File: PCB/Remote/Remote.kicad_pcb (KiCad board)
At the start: 2 copper layers, 104.1 x 104.1 mm, 27 parts, among them J1 Barrel_Jack, J2 Joystick (Servo), J3 Joystick (Motor), M1 MountingHole_3.5mm_Pad, M2 MountingHole_3.5mm_Pad, M3 MountingHole_3.5mm_Pad, M4 MountingHole_3.5mm_Pad, SW1 Reset Button, SW2 Auto/Manual, SW3 Siren on/off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

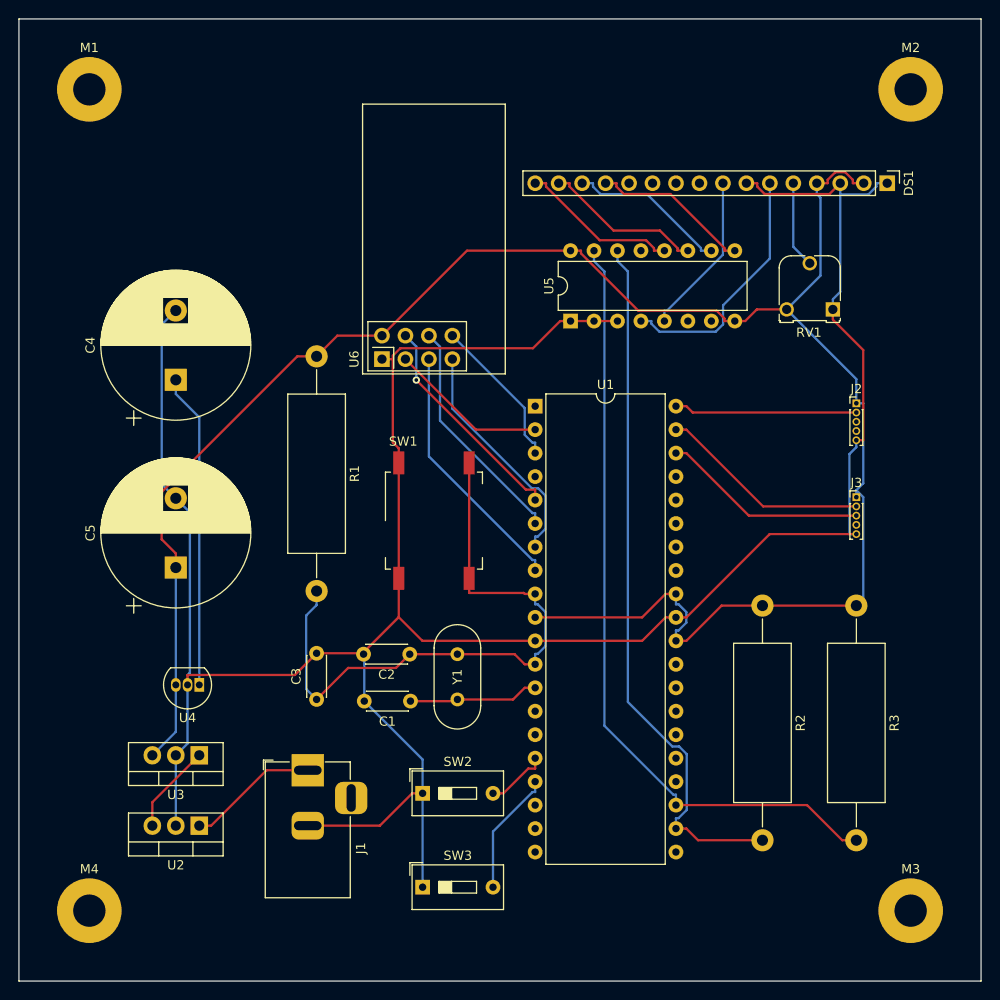
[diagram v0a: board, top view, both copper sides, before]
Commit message: 3.3v error in PCB
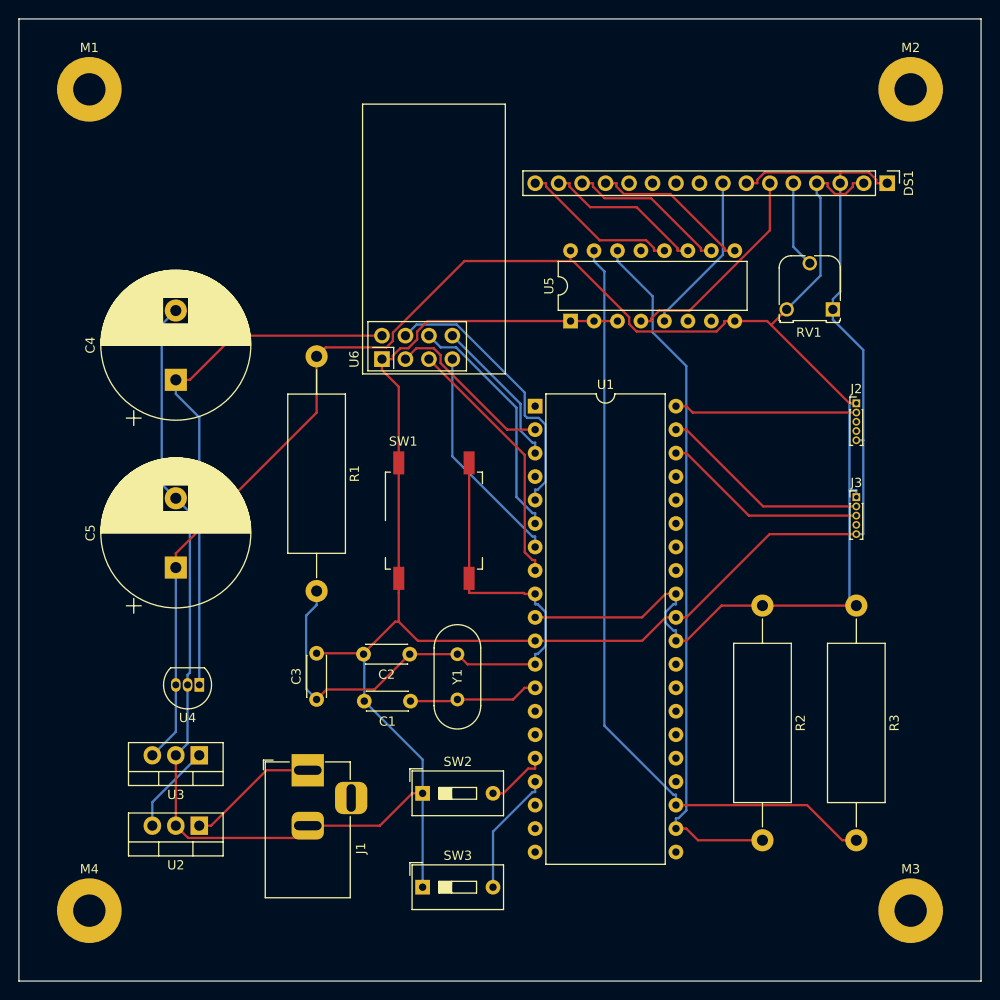
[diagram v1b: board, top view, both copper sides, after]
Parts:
- DS1: value HY1602E LCD 16x2 -> HY1602E
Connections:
- U6 pad 2: /Atmega32/5V -> /Power Supply/3.3V
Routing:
- net /Power Supply/3.3V: track 34.1 -> 58.4 mm
- net /Atmega32/CSN: track 24.2 -> 30.4 mm, vias 1 -> 0
- net Net-(DS1-Pad6): track 27.2 -> 23.3 mm
- net /Atmega32/CE: track 17.2 -> 18.7 mm
- net /Atmega32/MISO: track 25.5 -> 24.2 mm
- net /Atmega32/MOSI: track 25.3 -> 26.2 mm
- net /Atmega32/GND: track 296.3 -> 297.1 mm
- net /Atmega32/5V: track 215.9 -> 215.2 mm

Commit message: Add simulation
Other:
- board text added: "Group 47"
- board text added: "L1 Hardware Project"
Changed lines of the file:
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@@
   (gr_line (start 202.0797 139.69495) (end 97.9397 139.69495) (layer "Edge.Cuts") (width 0.1))
   (gr_line (start 202.0797 35.55495) (end 202.0797 139.69495) (layer "Edge.Cuts") (width 0.1))
+  (gr_text "Group 47" (at 171.5697 45.72) (layer "B.SilkS")
+    (effects (font (size 3 3) (thickness 0.3)) (justify mirror))
+  )
+  (gr_text "L1 Hardware Project" (at 170.18 40.64) (layer "B.SilkS")
+    (effects (font (size 2 2) (thickness 0.3)) (justify mirror))
+  )
+  (gr_text "Group 47" (at 116.84 55.88) (layer "F.SilkS")
+    (effects (font (size 3 3) (thickness 0.3)))
+  )
+  (gr_text "L1 Hardware Project" (at 116.84 50.8) (layer "F.SilkS")
+    (effects (font (size 2 2) (thickness 0.3)))
+  )
+  (dimension (type aligned) (layer "F.SilkS")
+    (pts (xy 194.4597 132.0749) (xy 194.4597 43.1749))
+    (height 13.8203)
+    (gr_text "88.9000 mm" (at 207.13 87.6249 90) (layer "F.SilkS")
+      (effects (font (size 1 1) (thickness 0.15)))
+    )
+    (format (units 3) (units_format 1) (precision 4))
+    (style (thickness 0.15) (arrow_length 1.27) (text_position_mode 0) (extension_height 0.58642) (extension_offset 0.5) keep_text_aligned)
+  )
+  (dimension (type aligned) (layer "F.SilkS")
+    (pts (xy 202.0797 35.55495) (xy 97.9397 35.55495))
+    (height 15.234949)
+    (gr_text "104.1400 mm" (at 150.0097 19.170001) (layer "F.SilkS")
+      (effects (font (size 1 1) (thickness 0.15)))
+    )
+    (format (units 3) (units_format 1) (precision 4))
+    (style (thickness 0.15) (arrow_length 1.27) (text_position_mode 0) (extension_height 0.58642) (extension_offset 0.5) keep_text_aligned)
+  )
+  (dimension (type aligned) (layer "F.SilkS")
+    (pts (xy 194.4597 43.1749) (xy 105.5597 43.1749))
+    (height 15.2349)
+    (gr_text "88.9000 mm" (at 150.0097 26.79) (layer "F.SilkS")
+      (effects (font (size 1 1) (thickness 0.15)))
+    )
+    (format (units 3) (units_format 1) (precision 4))
+    (style (thickness 0.15) (arrow_length 1.27) (text_position_mode 0) (extension_height 0.58642) (extension_offset 0.5) keep_text_aligned)
+  )
+  (dimension (type aligned) (layer "F.SilkS")
+    (pts (xy 202.0797 35.55495) (xy 194.4597 35.56))
+    (height 7.617572)
+    (gr_text "7.6200 mm" (at 198.26389 26.789905 0.03797160685) (layer "F.SilkS")
+      (effects (font (size 1 1) (thickness 0.15)))
+    )
+    (format (units 3) (units_format 1) (precision 4))
+    (style (thickness 0.15) (arrow_length 1.27) (text_position_mode 0) (extension_height 0.58642) (extension_offset 0.5) keep_text_aligned)
+  )
+  (dimension (type aligned) (layer "F.SilkS")
+    (pts (xy 198.12 139.69495) (xy 198.12 35.56))
+    (height 17.78)
+    (gr_text "104.1350 mm" (at 214.75 87.627475 90) (layer "F.SilkS")
+      (effects (font (size 1 1) (thickness 0.15)))
+    )
+    (format (units 3) (units_format 1) (precision 4))
+    (style (thickness 0.15) (arrow_length 1.27) (text_position_mode 0) (extension_height 0.58642) (extension_offset 0.5) keep_text_aligned)
+  )
+  (dimension (type aligned) (layer "F.SilkS")
+    (pts (xy 194.4597 43.1749) (xy 194.4597 35.56))
+    (height 13.8203)
+    (gr_text "7.6149 mm" (at 207.13 39.36745 90) (layer "F.SilkS")
+      (effects (font (size 1 1) (thickness 0.15)))
+    )
+    (format (units 3) (units_format 1) (precision 4))
+    (style (thickness 0.15) (arrow_length 1.27) (text_position_mode 0) (extension_height 0.58642) (extension_offset 0.5) keep_text_aligned)
+  )
   (segment (start 145.3997 109.2149) (end 151.4244 109.2149) (width 0.25) (layer "F.Cu") (net 1))
   (segment (start 151.4244 109.2149) (end 152.6894 107.9499) (width 0.25) (layer "F.Cu") (net 1))
